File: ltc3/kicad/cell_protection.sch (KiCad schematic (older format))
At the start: 80 parts, among them P301 CONN_BATT_MAIN, P303 CONN_BATT_SENSE, P305 S2BPHKS, P306 CONN_01X02, Q301 MMBT3904, Q302 SUM110P08-11, Q303 SUM110P08-11, Q304 SUM110P08-11, Q305 SUM110P08-11, Q306 NDS9407, U301 LTC2990, U302 BQ77PL900

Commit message: LTC3: Deleted "dummy" and "valve" footprint assignments.
The "dummy" footprints were meant for off-board components, but they
still found their way into the board layout as labels without any
pads, silkscreen, etc.

The "valve" footprints were meant as reminder placeholders of
components that still needed their final assignment.
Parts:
- BT301, BT302, BT303, BT304, BT305, BT306, BT307, BT308, P302, P304: footprint Oddities:Dummy_Empty -> (none)
- P301, P303: footprint Valves:VALVE-OCTAL -> (none)
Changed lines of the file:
@@
 LIBS:transistors
 LIBS:ttl_ieee
-LIBS:valves
 LIBS:video
 LIBS:Xicor
@@
 F 0 "P303" H 9650 6750 50  0000 C CNN
 F 1 "CONN_BATT_SENSE" V 9800 6300 50  0000 C CNN
-F 2 "Valves:VALVE-OCTAL" H 9650 6300 60  0001 C CNN
+F 2 "" H 9650 6300 60  0001 C CNN
 F 3 "" H 9650 6300 60  0000 C CNN
 	1    9650 6300
@@
 F 0 "P301" H 9650 5200 50  0000 C CNN
 F 1 "CONN_BATT_MAIN" V 9800 5050 50  0000 C CNN
-F 2 "Valves:VALVE-OCTAL" H 9650 5050 60  0001 C CNN
+F 2 "" H 9650 5050 60  0001 C CNN
 F 3 "" H 9650 5050 60  0000 C CNN
 	1    9650 5050
@@
 F 0 "P304" H 10350 6750 50  0000 C CNN
 F 1 "~" V 10450 6300 50  0000 C CNN
-F 2 "Oddities:Dummy_Empty" H 10350 6300 60  0001 C CNN
+F 2 "" H 10350 6300 60  0001 C CNN
 F 3 "" H 10350 6300 60  0000 C CNN
 	1    10350 6300
@@
 F 0 "P302" H 10350 5200 50  0000 C CNN
 F 1 "~" V 10450 5050 50  0000 C CNN
-F 2 "Oddities:Dummy_Empty" H 10350 5050 60  0001 C CNN
+F 2 "" H 10350 5050 60  0001 C CNN
 F 3 "" H 10350 5050 60  0000 C CNN
 	1    10350 5050
@@
 F 0 "BT301" H 11418 5850 50  0000 L CNN
 F 1 "~" H 11418 5804 50  0000 L CNN
-F 2 "Oddities:Dummy_Empty" V 11300 5860 60  0001 C CNN
+F 2 "" V 11300 5860 60  0001 C CNN
 F 3 "" V 11300 5860 60  0000 C CNN
 	1    11300 5850
@@
 F 0 "BT302" H 11418 6250 50  0000 L CNN
 F 1 "~" H 11418 6204 50  0000 L CNN
-F 2 "Oddities:Dummy_Empty" V 11300 6260 60  0001 C CNN
+F 2 "" V 11300 6260 60  0001 C CNN
 F 3 "" V 11300 6260 60  0000 C CNN
 	1    11300 6250
@@
 F 0 "BT303" H 11418 6650 50  0000 L CNN
 F 1 "~" H 11418 6604 50  0000 L CNN
-F 2 "Oddities:Dummy_Empty" V 11300 6660 60  0001 C CNN
+F 2 "" V 11300 6660 60  0001 C CNN
 F 3 "" V 11300 6660 60  0000 C CNN
 	1    11300 6650
@@
 F 0 "BT304" H 11418 7050 50  0000 L CNN
 F 1 "~" H 11418 7004 50  0000 L CNN
-F 2 "Oddities:Dummy_Empty" V 11300 7060 60  0001 C CNN
+F 2 "" V 11300 7060 60  0001 C CNN
 F 3 "" V 11300 7060 60  0000 C CNN
 	1    11300 7050
@@
 F 0 "BT305" H 11418 7450 50  0000 L CNN
 F 1 "~" H 11418 7404 50  0000 L CNN
-F 2 "Oddities:Dummy_Empty" V 11300 7460 60  0001 C CNN
+F 2 "" V 11300 7460 60  0001 C CNN
 F 3 "" V 11300 7460 60  0000 C CNN
 	1    11300 7450
@@
 F 0 "BT306" H 11418 7850 50  0000 L CNN
 F 1 "~" H 11418 7804 50  0000 L CNN
-F 2 "Oddities:Dummy_Empty" V 11300 7860 60  0001 C CNN
+F 2 "" V 11300 7860 60  0001 C CNN
 F 3 "" V 11300 7860 60  0000 C CNN
 	1    11300 7850
@@
 F 0 "BT307" H 11418 8250 50  0000 L CNN
 F 1 "~" H 11418 8204 50  0000 L CNN
-F 2 "Oddities:Dummy_Empty" V 11300 8260 60  0001 C CNN
+F 2 "" V 11300 8260 60  0001 C CNN
 F 3 "" V 11300 8260 60  0000 C CNN
 	1    11300 8250
@@
 F 0 "BT308" H 11418 8650 50  0000 L CNN
 F 1 "~" H 11418 8604 50  0000 L CNN
-F 2 "Oddities:Dummy_Empty" V 11300 8660 60  0001 C CNN
+F 2 "" V 11300 8660 60  0001 C CNN
 F 3 "" V 11300 8660 60  0000 C CNN
 	1    11300 8650

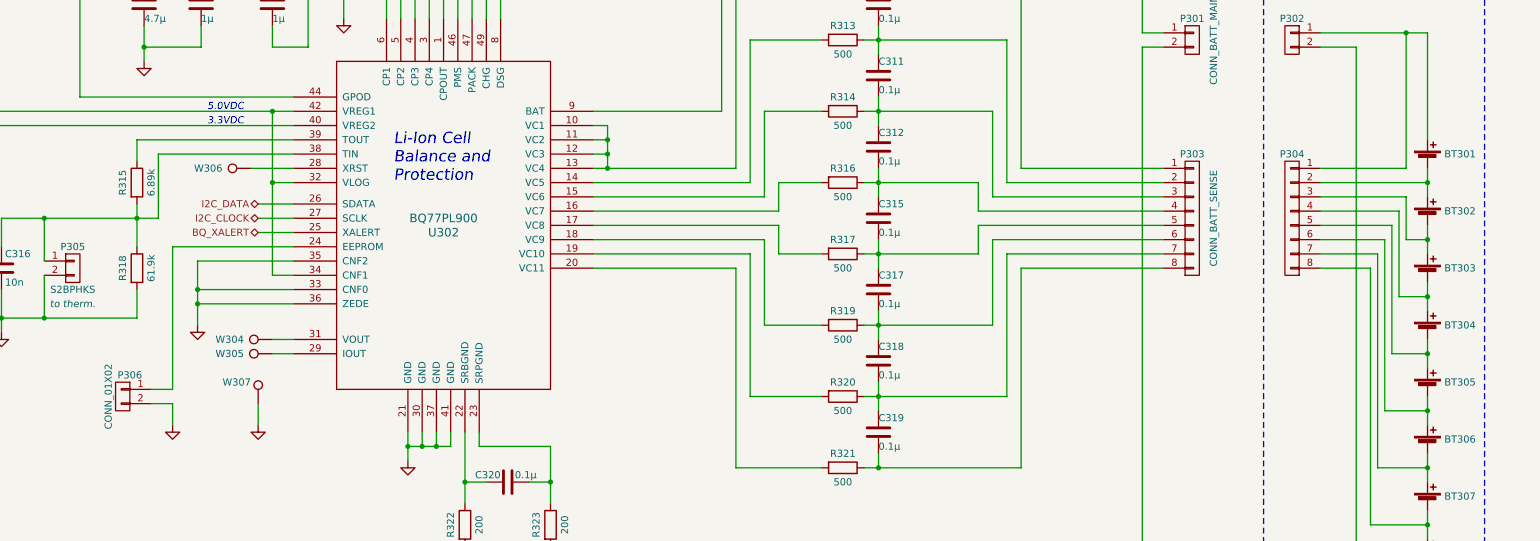
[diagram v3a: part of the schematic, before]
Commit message: LTC3: More footprint assignment.
Set footprint to "OFF-BOARD" for all off-board components.  This
results in an error dialog when opening the footprint assignment tool,
but it makes it obvious which components shouldn't have any footprint
assigned.
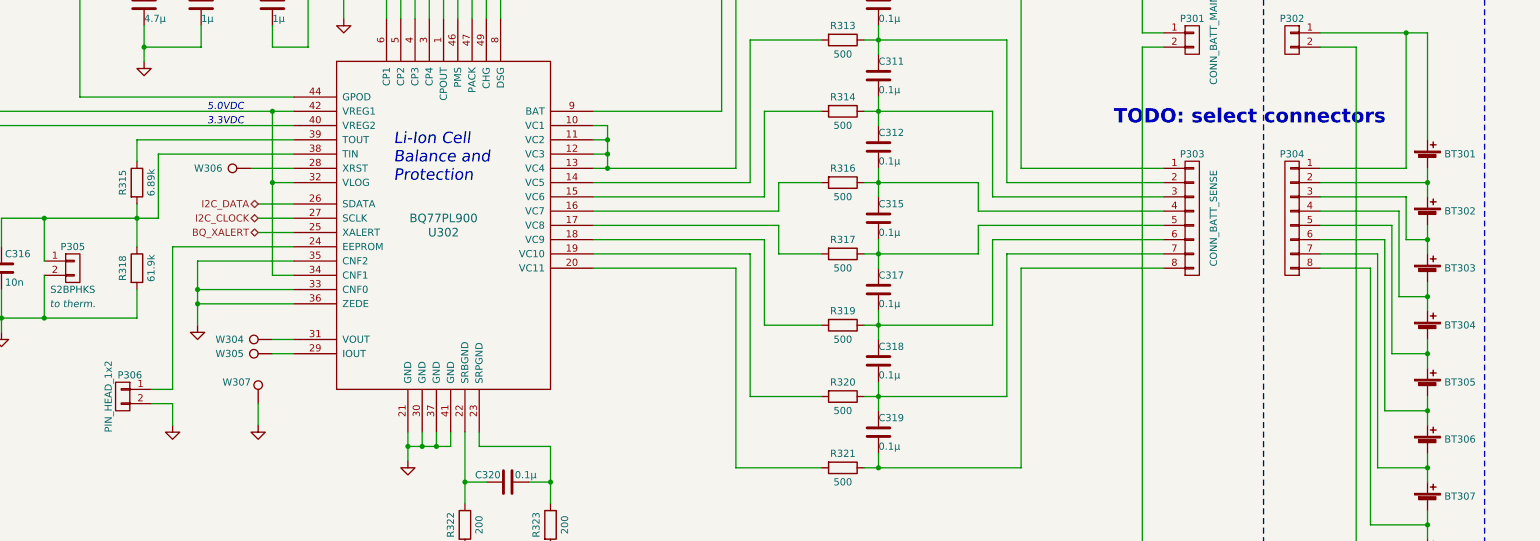
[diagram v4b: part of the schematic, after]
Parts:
- BT301, BT302, BT303, BT304, BT305, BT306, BT307, BT308, P302, P304: footprint (none) -> OFF-BOARD
- C304: footprint (none) -> Capacitors_SMD:C_0805
- P306: value CONN_01X02 -> PIN_HEAD_1x2
- Q306: footprint SO-8 -> Power_Integrations:SO-8
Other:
- note added: "TODO: select connectors"
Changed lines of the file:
@@
 LIBS:atmel
 LIBS:audio
+LIBS:bbd
 LIBS:brooktre
 LIBS:cmos4000
@@
 LIBS:transistors
 LIBS:ttl_ieee
-LIBS:video
-LIBS:Xicor
-LIBS:xilinx
-LIBS:Zilog
 LIBS:Launch_Tower_Computer_III-cache
 EELAYER 25 0
@@
 F 0 "P304" H 10350 6750 50  0000 C CNN
 F 1 "~" V 10450 6300 50  0000 C CNN
-F 2 "" H 10350 6300 60  0001 C CNN
+F 2 "OFF-BOARD" H 10350 6300 60  0001 C CNN
 F 3 "" H 10350 6300 60  0000 C CNN
 	1    10350 6300
@@
 F 0 "P302" H 10350 5200 50  0000 C CNN
 F 1 "~" V 10450 5050 50  0000 C CNN
-F 2 "" H 10350 5050 60  0001 C CNN
+F 2 "OFF-BOARD" H 10350 5050 60  0001 C CNN
 F 3 "" H 10350 5050 60  0000 C CNN
 	1    10350 5050
@@
 F 0 "BT301" H 11418 5850 50  0000 L CNN
 F 1 "~" H 11418 5804 50  0000 L CNN
-F 2 "" V 11300 5860 60  0001 C CNN
+F 2 "OFF-BOARD" V 11300 5860 60  0001 C CNN
 F 3 "" V 11300 5860 60  0000 C CNN
 	1    11300 5850
@@
 F 0 "BT302" H 11418 6250 50  0000 L CNN
 F 1 "~" H 11418 6204 50  0000 L CNN
-F 2 "" V 11300 6260 60  0001 C CNN
+F 2 "OFF-BOARD" V 11300 6260 60  0001 C CNN
 F 3 "" V 11300 6260 60  0000 C CNN
 	1    11300 6250
@@
 F 0 "BT303" H 11418 6650 50  0000 L CNN
 F 1 "~" H 11418 6604 50  0000 L CNN
-F 2 "" V 11300 6660 60  0001 C CNN
+F 2 "OFF-BOARD" V 11300 6660 60  0001 C CNN
 F 3 "" V 11300 6660 60  0000 C CNN
 	1    11300 6650
@@
 F 0 "BT304" H 11418 7050 50  0000 L CNN
 F 1 "~" H 11418 7004 50  0000 L CNN
-F 2 "" V 11300 7060 60  0001 C CNN
+F 2 "OFF-BOARD" V 11300 7060 60  0001 C CNN
 F 3 "" V 11300 7060 60  0000 C CNN
 	1    11300 7050
@@
 F 0 "BT305" H 11418 7450 50  0000 L CNN
 F 1 "~" H 11418 7404 50  0000 L CNN
-F 2 "" V 11300 7460 60  0001 C CNN
+F 2 "OFF-BOARD" V 11300 7460 60  0001 C CNN
 F 3 "" V 11300 7460 60  0000 C CNN
 	1    11300 7450
@@
 F 0 "BT306" H 11418 7850 50  0000 L CNN
 F 1 "~" H 11418 7804 50  0000 L CNN
-F 2 "" V 11300 7860 60  0001 C CNN
+F 2 "OFF-BOARD" V 11300 7860 60  0001 C CNN
 F 3 "" V 11300 7860 60  0000 C CNN
 	1    11300 7850
@@
 F 0 "BT307" H 11418 8250 50  0000 L CNN
 F 1 "~" H 11418 8204 50  0000 L CNN
-F 2 "" V 11300 8260 60  0001 C CNN
+F 2 "OFF-BOARD" V 11300 8260 60  0001 C CNN
 F 3 "" V 11300 8260 60  0000 C CNN
 	1    11300 8250
@@
 F 0 "BT308" H 11418 8650 50  0000 L CNN
 F 1 "~" H 11418 8604 50  0000 L CNN
-F 2 "" V 11300 8660 60  0001 C CNN
+F 2 "OFF-BOARD" V 11300 8660 60  0001 C CNN
 F 3 "" V 11300 8660 60  0000 C CNN
 	1    11300 8650
@@
 P 2150 7550
 F 0 "P306" H 2100 7700 50  0000 C CNN
-F 1 "CONN_01X02" V 2250 7550 50  0000 C CNN
+F 1 "PIN_HEAD_1x2" V 2250 7550 50  0000 C CNN
 F 2 "Pin_Headers:Pin_Header_Straight_1x02" H 2150 7550 60  0001 C CNN
 F 3 "" H 2150 7550 60  0000 C CNN
@@
 F 0 "C304" H 6350 2550 50  0000 L CNN
 F 1 "4.7n" H 6350 2350 50  0000 L CNN
-F 2 "" H 6388 2300 50  0000 C CNN
+F 2 "Capacitors_SMD:C_0805" H 6388 2300 50  0001 C CNN
 F 3 "" H 6350 2450 50  0000 C CNN
 	1    6350 2450
@@
 F 0 "Q306" V 4478 1350 50  0000 C CNN
 F 1 "NDS9407" V 4387 1350 50  0000 C CNN
-F 2 "SO-8" H 4400 1305 50  0001 L CNN
+F 2 "Power_Integrations:SO-8" H 4400 1305 50  0001 L CNN
 F 3 "" H 4150 1350 50  0000 L CNN
 	1    3950 1400
@@
 Wire Wire Line
 	2100 3100 2100 3000
+Text Notes 9100 5650 0    100  ~ 20
+TODO: select connectors
 $EndSCHEMATC

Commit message: More of the same.
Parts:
- P301: footprint (none) -> Connectors_Molex:Molex_Microfit3_Header_02x01_Straight_43045-0228
- P303: footprint (none) -> Connectors_Molex:Molex_Microfit3_Header_02x04_Straight_43045-0828
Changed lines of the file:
@@
 F 0 "P303" H 9650 6750 50  0000 C CNN
 F 1 "CONN_BATT_SENSE" V 9800 6300 50  0000 C CNN
-F 2 "" H 9650 6300 60  0001 C CNN
+F 2 "Connectors_Molex:Molex_Microfit3_Header_02x04_Straight_43045-0828" H 9650 6300 60  0001 C CNN
 F 3 "" H 9650 6300 60  0000 C CNN
 	1    9650 6300
@@
 F 0 "P301" H 9650 5200 50  0000 C CNN
 F 1 "CONN_BATT_MAIN" V 9800 5050 50  0000 C CNN
-F 2 "" H 9650 5050 60  0001 C CNN
+F 2 "Connectors_Molex:Molex_Microfit3_Header_02x01_Straight_43045-0228" H 9650 5050 60  0001 C CNN
 F 3 "" H 9650 5050 60  0000 C CNN
 	1    9650 5050
